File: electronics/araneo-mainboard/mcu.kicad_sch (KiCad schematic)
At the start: 17 parts, among them J9 GPIO, SW2 BUTTON, SW3 RESET

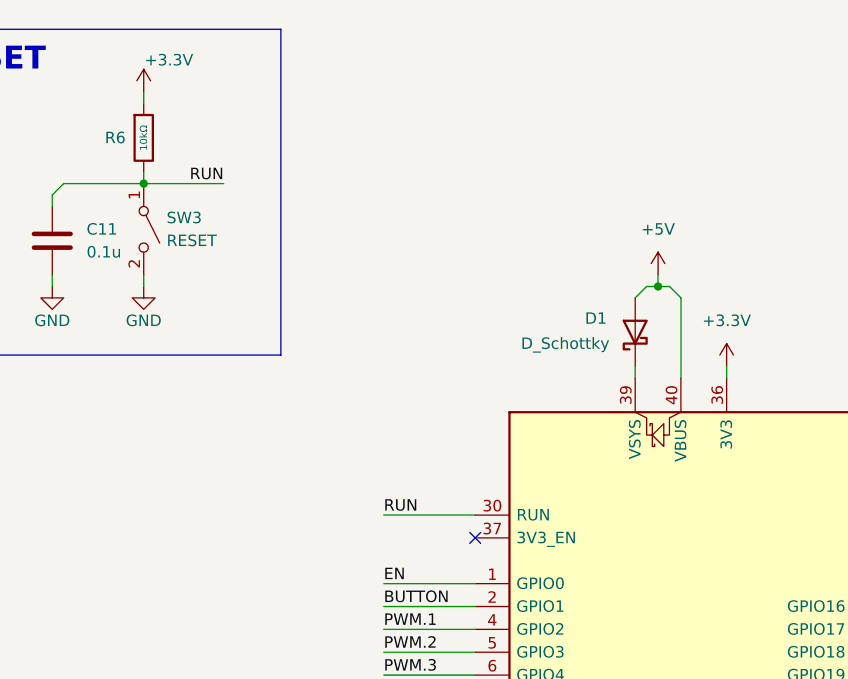
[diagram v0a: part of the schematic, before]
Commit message: add components schematics
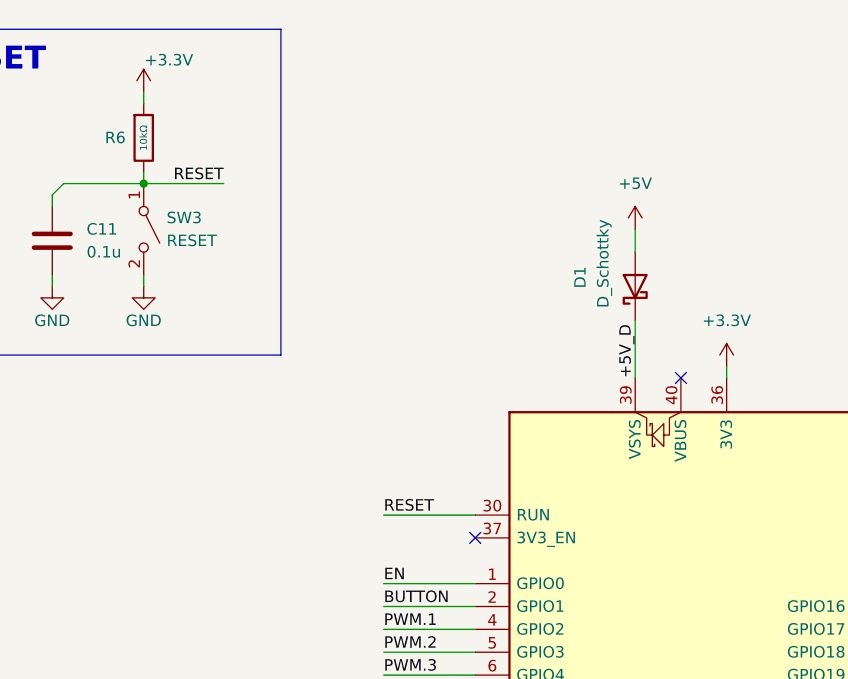
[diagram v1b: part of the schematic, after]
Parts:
- D1: footprint Diode_THT:D_DO-35_SOD27_P7.62mm_Horizontal -> (none)
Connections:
- net +5V: no longer A1.40 (VBUS)
- net +5V_D: now reaches A1.39 (VSYS), D1.1 (K)
- net RUN renamed RESET
- no-connect marks 1 -> 2

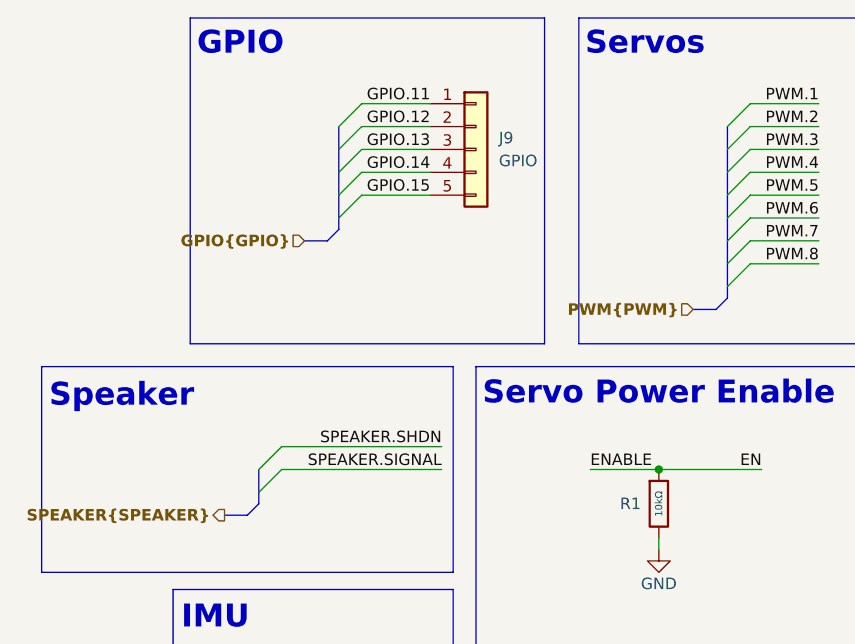
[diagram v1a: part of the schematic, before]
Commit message: add speaker schematic
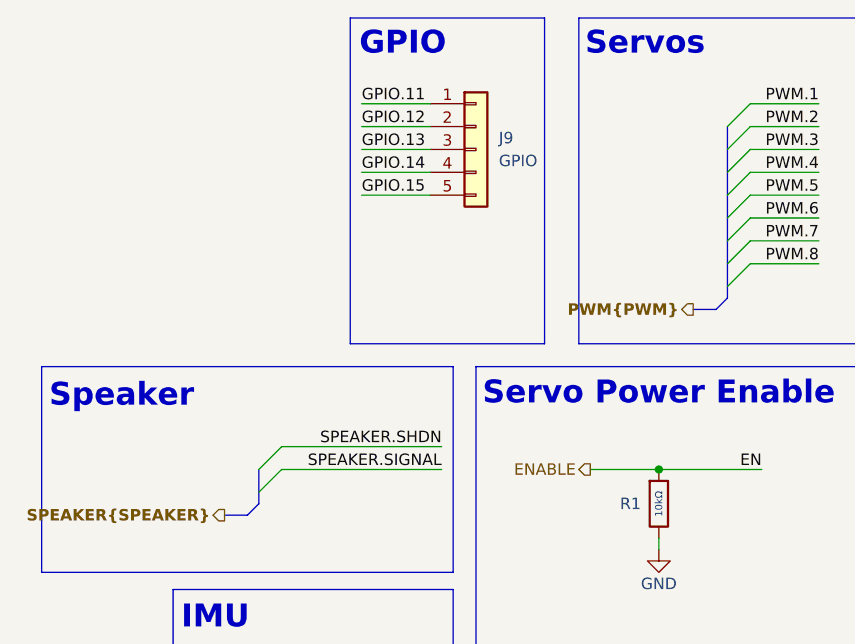
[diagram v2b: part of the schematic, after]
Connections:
- net EN renamed ENABLE

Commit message: electronics: assign footprints
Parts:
- C10, C11: footprint PCM_JLCPCB:R_0402 -> PCM_JLCPCB:C_0402
- C9: footprint PCM_JLCPCB:R_0603 -> PCM_JLCPCB:C_0603
- D1: footprint (none) -> PCM_JLCPCB:D_0603
- D2: footprint PCM_SparkFun-LED:LED_0603_1608Metric -> PCM_JLCPCB:D_0603
- R7: footprint PCM_JLCPCB:R_0402 -> PCM_JLCPCB:R_0603
- SW2: footprint Button_Switch_SMD:Nidec_Copal_CAS-120A -> PCM_SparkFun-Connector:ScrewTerminal_1x02_P3.5mm_Blue
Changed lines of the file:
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@@
 			)
 		)
-		(property "Footprint" "PCM_JLCPCB:R_0402"
+		(property "Footprint" "PCM_JLCPCB:C_0402"
 			(at 70.8152 41.91 0)
 			(hide yes)
@@
 			)
 		)
-		(property "Footprint" "PCM_JLCPCB:R_0402"
+		(property "Footprint" "PCM_JLCPCB:C_0402"
 			(at 23.8252 43.18 0)
 			(hide yes)
@@
 			)
 		)
-		(property "Footprint" "Button_Switch_SMD:Nidec_Copal_CAS-120A"
+		(property "Footprint" "PCM_SparkFun-Connector:ScrewTerminal_1x02_P3.5mm_Blue"
 			(at 33.02 38.1 0)
 			(hide yes)
@@
 			)
 		)
-		(property "Footprint" "PCM_JLCPCB:R_0603"
+		(property "Footprint" "PCM_JLCPCB:C_0603"
 			(at 268.9352 154.94 0)
 			(hide yes)
@@
 			)
 		)
-		(property "Footprint" "PCM_SparkFun-LED:LED_0603_1608Metric"
+		(property "Footprint" "PCM_JLCPCB:D_0603"
 			(at 34.29 63.5 0)
 			(hide yes)
@@
 			)
 		)
-		(property "Footprint" ""
+		(property "Footprint" "PCM_JLCPCB:D_0603"
 			(at 134.62 43.18 0)
 			(hide yes)
@@
 			)
 		)
-		(property "Footprint" "PCM_JLCPCB:R_0402"
+		(property "Footprint" "PCM_JLCPCB:R_0603"
 			(at 26.67 70.358 90)
 			(hide yes)

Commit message: add first layout
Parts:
- SW3: footprint Button_Switch_SMD:Nidec_Copal_CAS-120A -> Button_Switch_SMD:SW_SPST_TL3305B
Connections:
- net BUTTON: now also C10.1, R5.2, SW2.1 (A)
- net LED_A: now reaches D2.2 (A), R7.2
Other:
- moved on the sheet: D2
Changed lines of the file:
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@@
 	(wire
 		(pts
-			(xy 39.37 69.85) (xy 38.1 68.58)
+			(xy 48.26 69.85) (xy 46.99 68.58)
 		)
 		(stroke
@@
 	(wire
 		(pts
-			(xy 39.37 69.85) (xy 39.37 71.12)
+			(xy 48.26 69.85) (xy 48.26 71.12)
 		)
 		(stroke
@@
 	(wire
 		(pts
-			(xy 30.48 68.58) (xy 31.75 68.58)
+			(xy 30.48 68.58) (xy 39.37 68.58)
 		)
 		(stroke
@@
 	(wire
 		(pts
+			(xy 44.45 68.58) (xy 46.99 68.58)
+		)
+		(stroke
+			(width 0)
+			(type default)
+		)
+	)
+	(wire
+		(pts
 			(xy 218.44 85.09) (xy 237.49 85.09)
 		)
@@
 	(wire
 		(pts
-			(xy 36.83 68.58) (xy 38.1 68.58)
-		)
-		(stroke
-			(width 0)
-			(type default)
-		)
-	)
-	(wire
-		(pts
 			(xy 80.01 30.48) (xy 80.01 31.75)
 		)
@@
 		)
 	)
+	(label "LED_K"
+		(at 45.72 68.58 0)
+		(effects
+			(font
+				(size 1.27 1.27)
+			)
+			(justify left bottom)
+		)
+	)
 	(label "PWM.7"
 		(at 279.4 38.1 180)
@@
 		)
 	)
+	(label "BUTTON"
+		(at 33.02 33.02 0)
+		(effects
+			(font
+				(size 1.27 1.27)
+			)
+			(justify left bottom)
+		)
+	)
 	(label "SPEAKER.SIGNAL"
 		(at 182.88 91.44 180)
@@
 		)
 	)
+	(label "LED_A"
+		(at 33.02 68.58 0)
+		(effects
+			(font
+				(size 1.27 1.27)
+			)
+			(justify left bottom)
+		)
+	)
 	(label "PWM.3"
 		(at 279.4 27.94 180)
@@
 	(symbol
 		(lib_id "PCM_SparkFun-PowerSymbol:GND")
-		(at 39.37 71.12 0)
+		(at 48.26 71.12 0)
 		(unit 1)
 		(body_style 1)
@@
 		(fields_autoplaced yes)
 		(property "Reference" "#PWR042"
-			(at 39.37 77.47 0)
+			(at 48.26 77.47 0)
 			(hide yes)
 			(show_name no)
@@
 		)
 		(property "Value" "GND"
-			(at 39.37 74.93 0)
+			(at 48.26 74.93 0)
 			(show_name no)
 			(do_not_autoplace yes)
@@
 		)
 		(property "Footprint" ""
-			(at 39.37 71.12 0)
+			(at 48.26 71.12 0)
 			(hide yes)
 			(show_name no)
@@
 		)
 		(property "Datasheet" ""
-			(at 39.37 71.12 0)
+			(at 48.26 71.12 0)
 			(hide yes)
 			(show_name no)
@@
 		)
 		(property "Description" "Power symbol creates a global label with name \"GND\" , ground"
-			(at 39.37 80.01 0)
+			(at 48.26 80.01 0)
 			(hide yes)
 			(show_name no)
@@
 			)
 		)
-		(property "Footprint" "Button_Switch_SMD:Nidec_Copal_CAS-120A"
+		(property "Footprint" "Button_Switch_SMD:SW_SPST_TL3305B"
 			(at 80.01 36.83 0)
 			(hide yes)
@@
 	(symbol
 		(lib_id "PCM_SparkFun-LED:LED")
-		(at 34.29 68.58 180)
+		(at 41.91 68.58 180)
 		(unit 1)
 		(body_style 1)
@@
 		(fields_autoplaced yes)
 		(property "Reference" "D2"
-			(at 34.2265 62.23 0)
+			(at 41.8465 62.23 0)
 			(show_name no)
 			(do_not_autoplace no)
@@
 		)
 		(property "Value" "LED"
-			(at 34.2265 64.77 0)
+			(at 41.8465 64.77 0)
 			(show_name no)
 			(do_not_autoplace no)
@@
 		)
 		(property "Footprint" "PCM_JLCPCB:D_0603"
-			(at 34.29 63.5 0)
+			(at 41.91 63.5 0)
 			(hide yes)
 			(show_name no)
@@
 		)
 		(property "Datasheet" ""
-			(at 34.29 60.96 0)
+			(at 41.91 60.96 0)
 			(hide yes)
 			(show_name no)
@@
 		)
 		(property "Description" "Light emitting diode"
-			(at 34.29 55.88 0)
+			(at 41.91 55.88 0)
 			(hide yes)
 			(show_name no)
@@
 		)
 		(property "PROD_ID" "LED-"
-			(at 34.29 58.42 0)
+			(at 41.91 58.42 0)
 			(hide yes)
 			(show_name no)

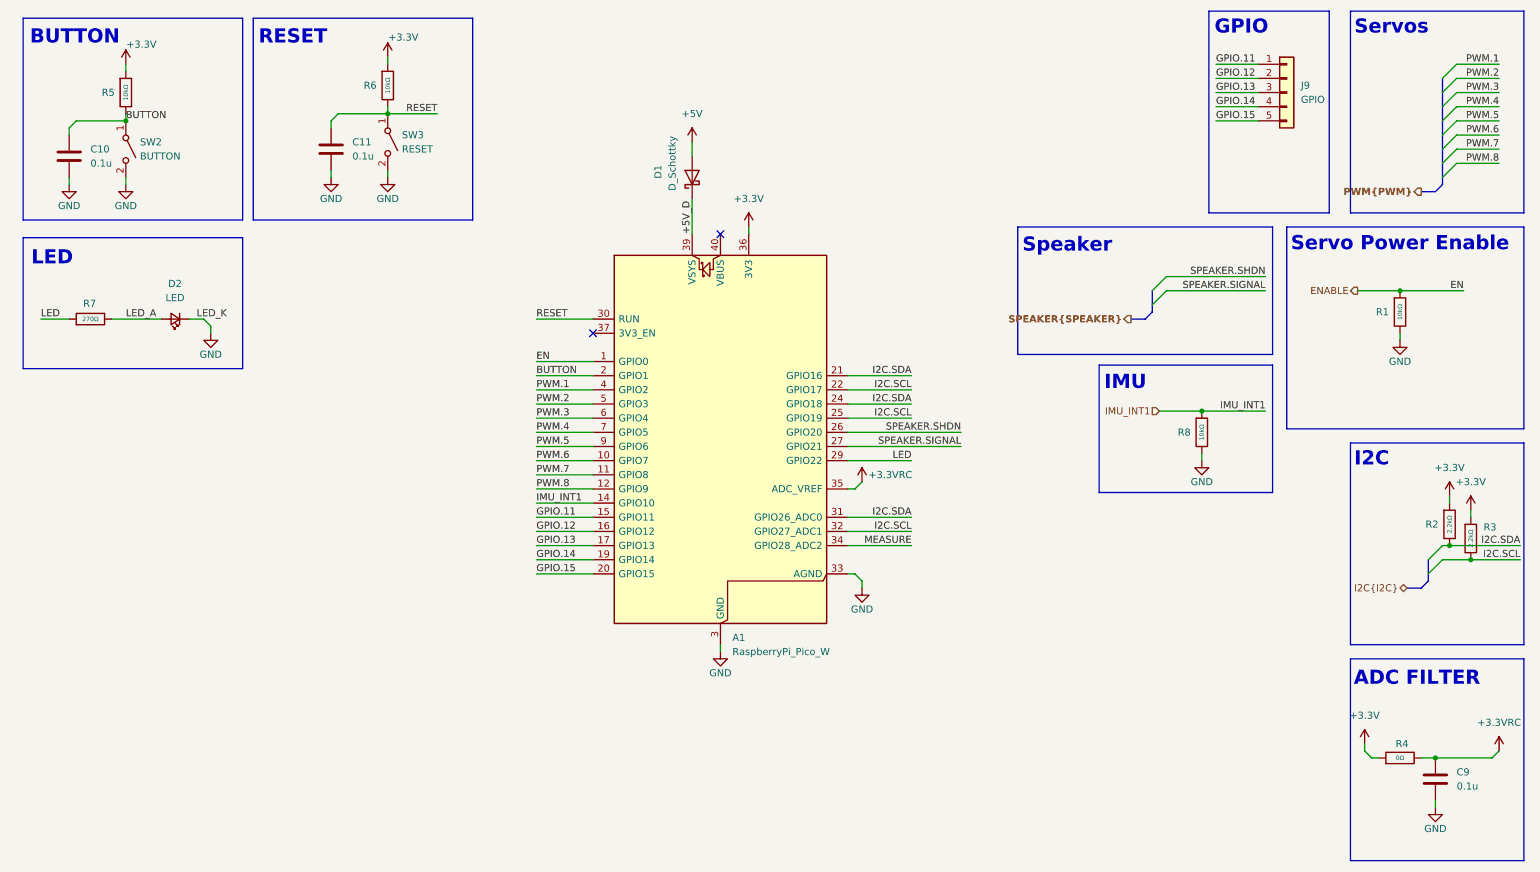
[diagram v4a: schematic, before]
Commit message: add missing components
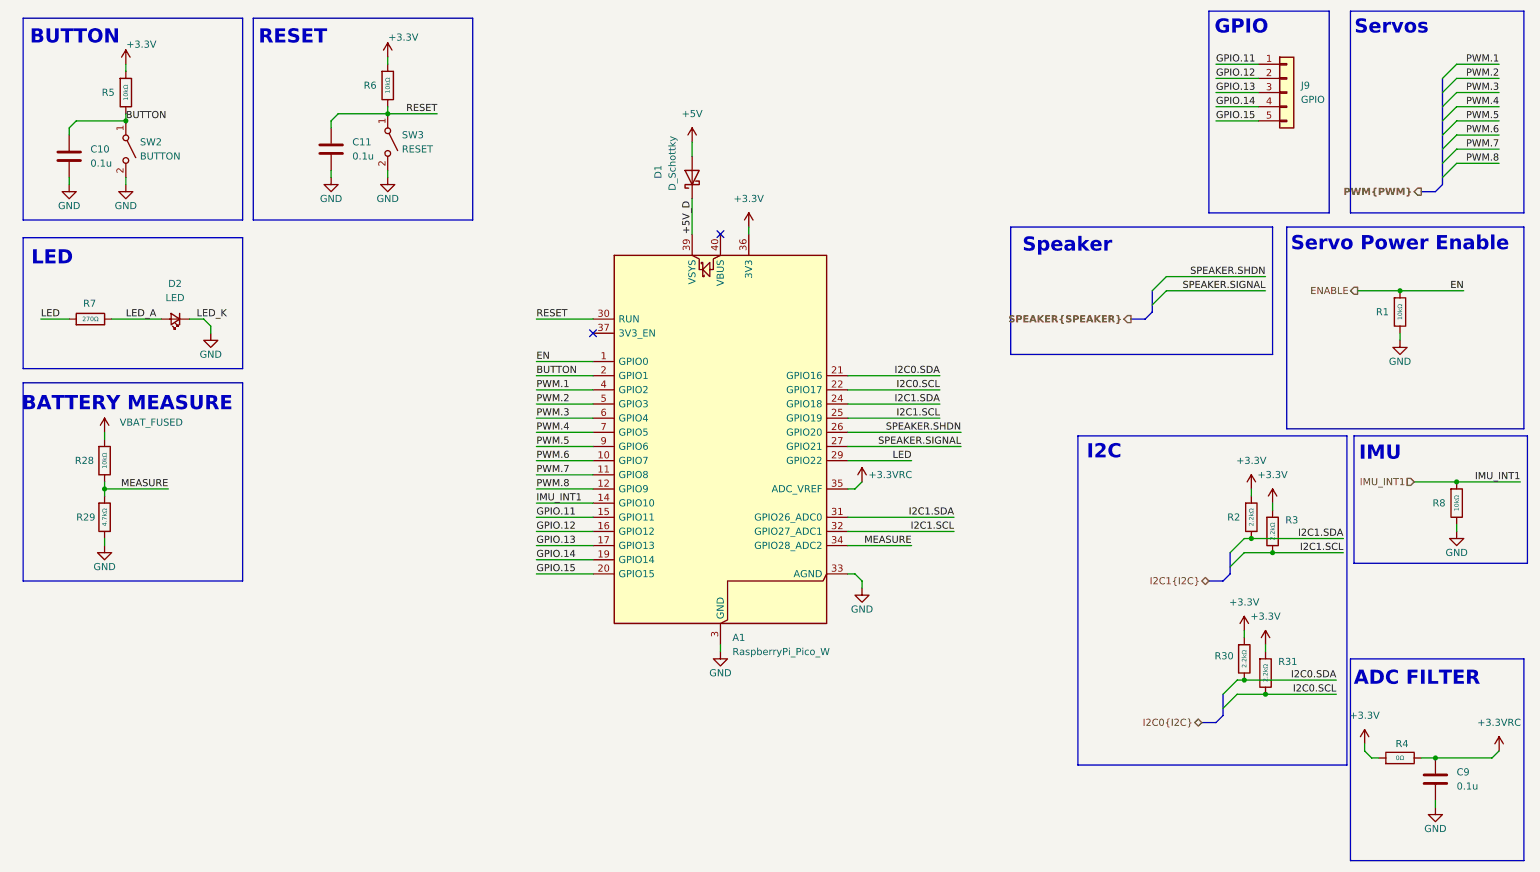
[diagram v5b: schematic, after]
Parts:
- added R28: 10kΩ, PCM_JLCPCB:R_0402, symbol PCM_JLCPCB-Resistors:0402,1.2kΩ
- added R29: 4.7kΩ, PCM_JLCPCB:R_0402, symbol PCM_JLCPCB-Resistors:0402,1.2kΩ
- added R30, R31: 2.2kΩ, PCM_JLCPCB:R_0402, symbol PCM_JLCPCB-Resistors:0402,1.2kΩ
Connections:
- net +3.3V: now also R30.1, R31.1
- net GND: now also R29.2
- net MEASURE: now also R28.2, R29.1
- net I2C.SCL renamed I2C1.SCL
- net I2C1.SCL: no longer A1.22 (GPIO17)
- net I2C.SDA renamed I2C1.SDA
- net I2C1.SDA: no longer A1.21 (GPIO16)
- new net I2C0.SCL: A1.22 (GPIO17), R31.2
- new net I2C0.SDA: A1.21 (GPIO16), R30.2
- new net VBAT_FUSED: R28.1
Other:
- note added: "BATTERY MEASURE"

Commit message: electronics: update bom
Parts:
- A1, D2, J9, SW2, SW3: now left out of the parts list
- R2, R3, R30, R31: value 2.2kΩ -> 4.7kΩ
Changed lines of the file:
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@@
 		(body_style 1)
 		(exclude_from_sim no)
-		(in_bom yes)
+		(in_bom no)
 		(on_board yes)
 		(in_pos_files yes)
@@
 			)
 		)
-		(property "Value" "2.2kΩ"
+		(property "Value" "4.7kΩ"
 			(at 234.95 104.14 90)
 			(show_name no)
@@
 		(body_style 1)
 		(exclude_from_sim no)
-		(in_bom yes)
+		(in_bom no)
 		(on_board yes)
 		(in_pos_files yes)
@@
 		(body_style 1)
 		(exclude_from_sim no)
-		(in_bom yes)
+		(in_bom no)
 		(on_board yes)
 		(in_pos_files yes)
@@
 		(body_style 1)
 		(exclude_from_sim no)
-		(in_bom yes)
+		(in_bom no)
 		(on_board yes)
 		(in_pos_files yes)
@@
 			)
 		)
-		(property "Value" "2.2kΩ"
+		(property "Value" "4.7kΩ"
 			(at 233.68 129.54 90)
 			(show_name no)
@@
 			)
 		)
-		(property "Value" "2.2kΩ"
+		(property "Value" "4.7kΩ"
 			(at 238.76 106.68 90)
 			(show_name no)
@@
 		(body_style 1)
 		(exclude_from_sim no)
-		(in_bom yes)
+		(in_bom no)
 		(on_board yes)
 		(in_pos_files yes)
@@
 			)
 		)
-		(property "Value" "2.2kΩ"
+		(property "Value" "4.7kΩ"
 			(at 237.49 132.08 90)
 			(show_name no)
